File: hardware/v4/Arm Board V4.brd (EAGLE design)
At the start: 114.3 x 50.8 mm, 57 parts, among them IC3 L6206D, U1 SN74LS241DW, U2 XBEE-1B3, U3 LSM9DS0

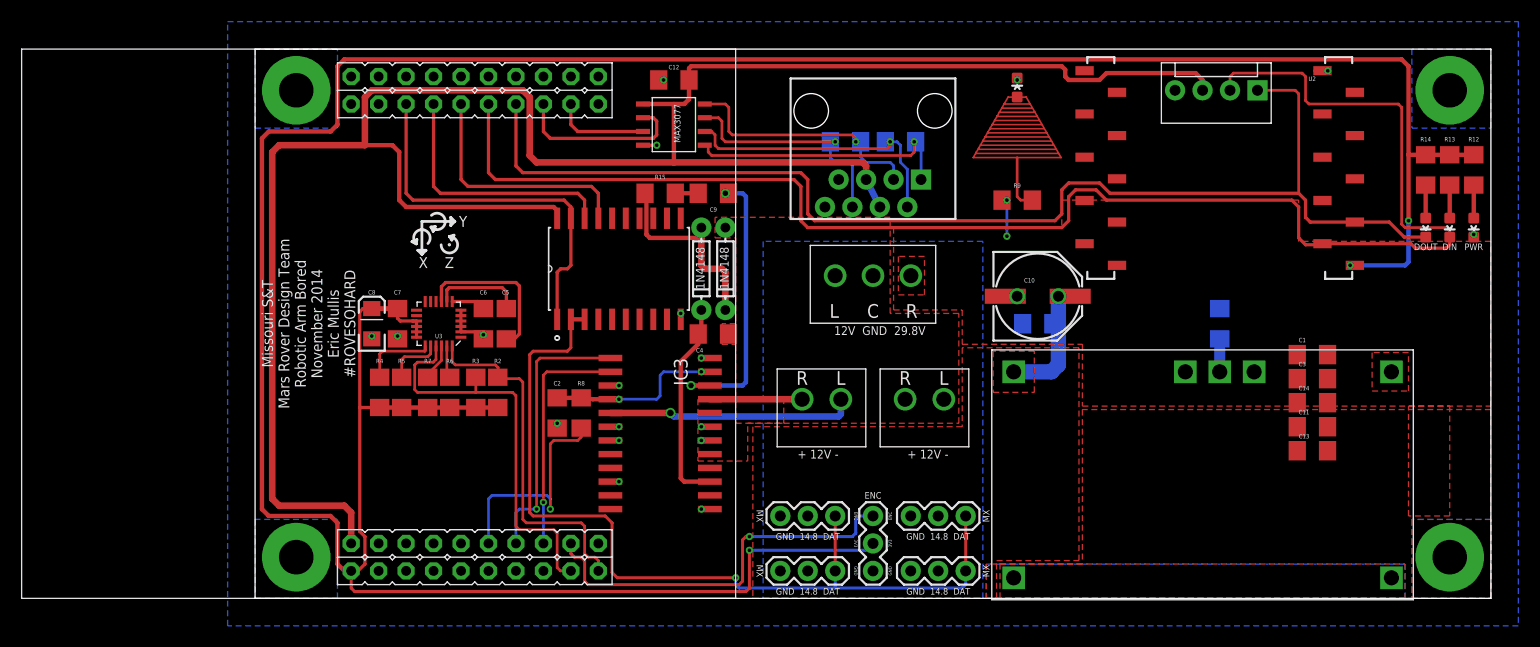
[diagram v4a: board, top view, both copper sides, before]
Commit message: Positioned all the caps correctly
I think the board is finished but may change as I look for parts to make
sure everything is correct
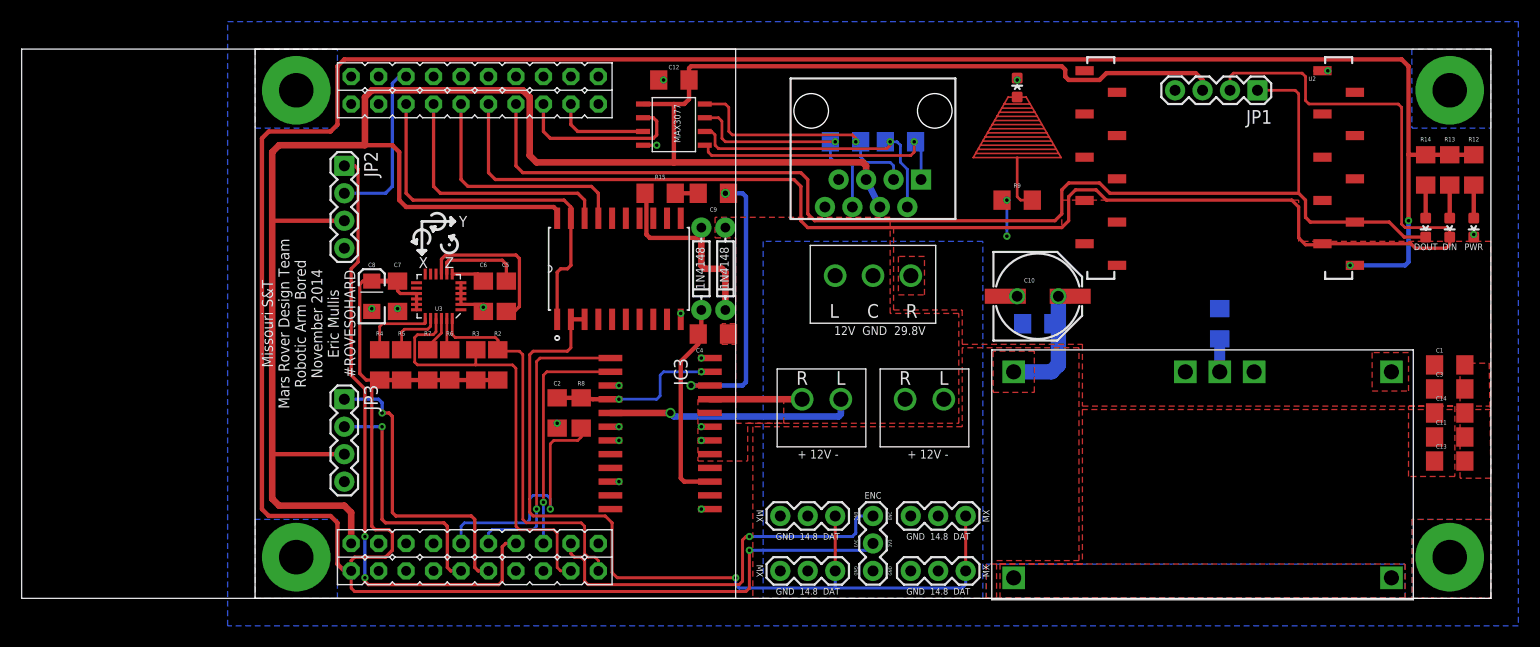
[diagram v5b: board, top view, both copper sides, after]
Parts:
- added JP2, JP3: (no value), SparkFun-Connectors:1X04
- JP1: device SparkFun-Connectors:MOLEX-1X4 -> SparkFun-Connectors:1X04
- moved C1 12.7 mm to (110.5, 21.6)
- moved C11 12.7 mm to (110.5, 14.9)
- moved C13 12.7 mm to (110.5, 12.7)
- moved C14 12.7 mm to (110.5, 17.1)
- moved C3 12.7 mm to (110.5, 19.4)
- moved C5 2.54 mm to (23.2, 27.9)
- moved C6 2.54 mm to (21.1, 27.9)
- moved C7 2.54 mm to (13.2, 27.9)
- moved C8 2.54 mm to (10.8, 27.9)
- moved U3 2.54 mm to (17.0, 27.9)
- moved R2 2.54 mm to (22.4, 21.6)
- moved R3 2.54 mm to (20.4, 21.6)
- moved R4 2.54 mm to (11.5, 21.6)
- moved R5 2.54 mm to (13.6, 21.6)
- moved R6 2.54 mm to (18.0, 21.6)
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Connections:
- new net RX_7: JP2.2, U$1.PE0
- new net TX_7: JP2.1, U$1.PE1
- net +5V: now also JP2.3, JP3.3
- net EN_A: now also U$1.PD2; no longer U$1.PD3
- net GND: now also JP2.4, JP3.4
- net IN1_A: now also U$1.PD3; no longer U$1.PE1
- net RX_5: now also JP3.2
- net TX_5: now also JP3.1
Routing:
- net TX_7: track 0.00 -> 57.8 mm, vias 0 -> 2
- net TX_5: track 0.00 -> 28.3 mm, vias 0 -> 1
- net RX_5: track 0.00 -> 23.6 mm, vias 0 -> 1
- net RX_7: track 0.00 -> 15.8 mm
- net +5V: track 199.1 -> 212.4 mm
- net +3V3: track 293.9 -> 298.6 mm
- net SDA: track 33.4 -> 35.9 mm
- net SCL: track 37.4 -> 40.0 mm
- net IN1_A: track 25.5 -> 27.9 mm
- net EN_A: track 21.0 -> 23.2 mm
- net GND: track 16.9 -> 18.0 mm

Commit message: Cleaned up the part names
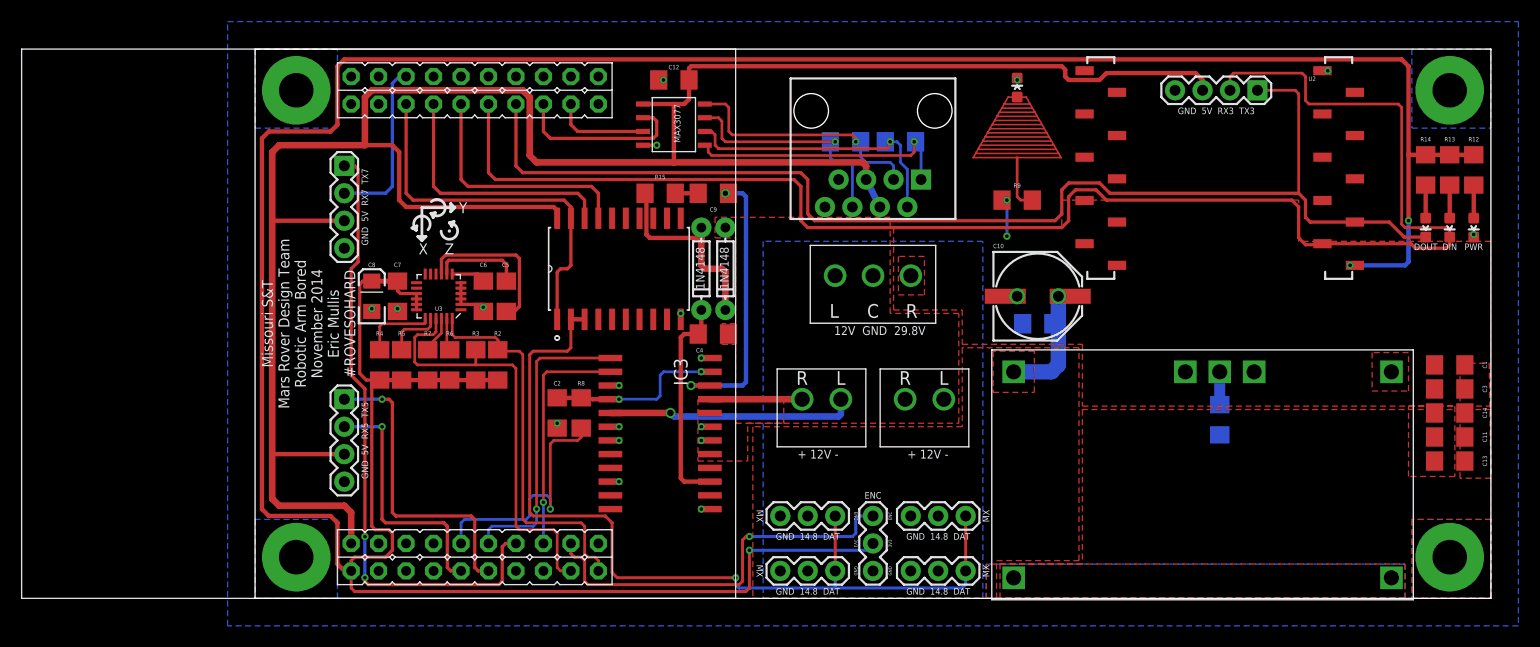
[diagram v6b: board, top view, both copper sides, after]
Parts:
- moved R1 8.89 mm to (89.2, 16.5), turned to 90 degrees
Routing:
- net VBOOT: track 20.1 -> 20.9 mm
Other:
- board text added: "GND 5V RX3 TX3"
- board text added: "GND 5V RX5 TX5"
- board text added: "GND 5V RX7 TX7"

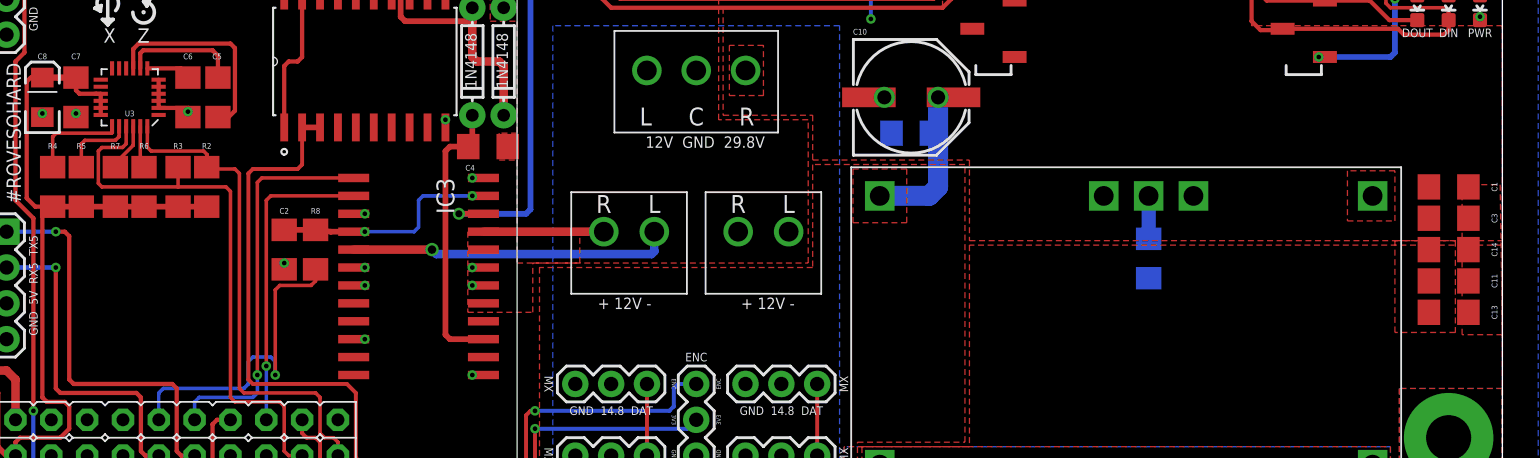
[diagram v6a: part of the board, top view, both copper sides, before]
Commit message: Added Mars Rover Bit Mip
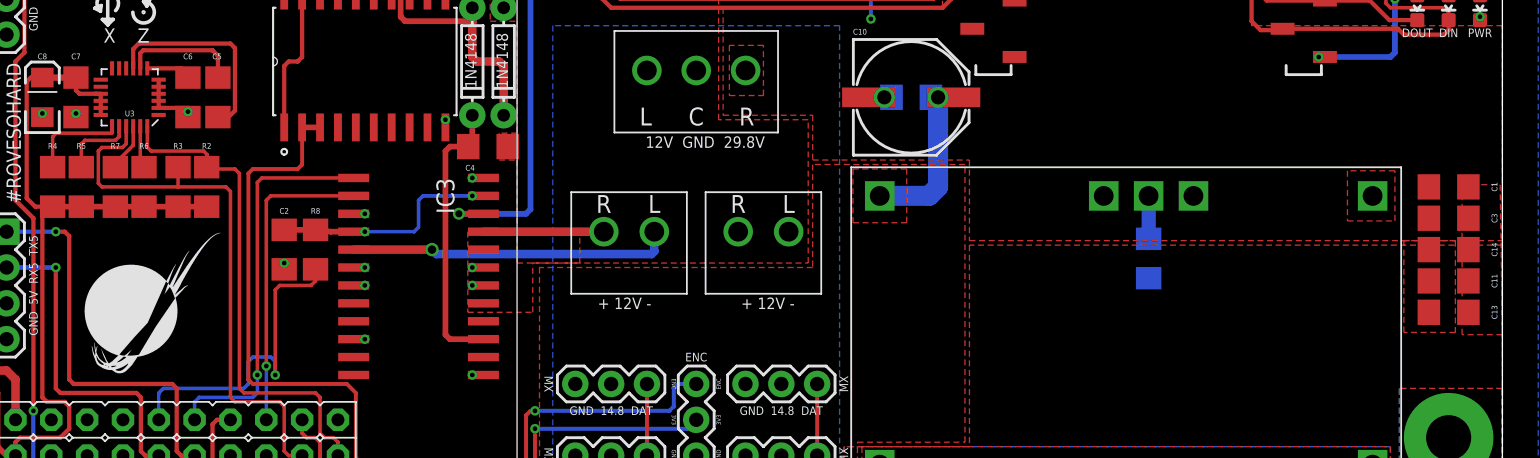
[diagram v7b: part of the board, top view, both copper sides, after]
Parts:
- moved C15 2.54 mm to (72.4, 27.9)

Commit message: 32u4 Xbee Shield
32u4 Xbee Shield
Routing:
- net 14.8V: track 12.4 -> 1.57 mm
- added copper zone on layer 16, net 14.8V
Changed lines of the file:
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@@
 <setting verticaltext="up"/>
 </settings>
-<grid distance="0.05" unitdist="inch" unit="inch" style="lines" multiple="1" display="yes" altdistance="0.0125" altunitdist="inch" altunit="inch"/>
+<grid distance="0.05" unitdist="inch" unit="inch" style="lines" multiple="1" display="yes" altdistance="0.00625" altunitdist="inch" altunit="inch"/>
 <layers>
 <layer number="1" name="Top" color="4" fill="1" visible="yes" active="yes"/>
@@
 <contactref element="JP1" pad="4"/>
 <contactref element="C10" pad="-"/>
-<via x="70.485" y="27.94" extent="1-16" drill="1" shape="square"/>
+<via x="70.64375" y="27.94" extent="1-16" drill="1" shape="square"/>
 <contactref element="C1" pad="2"/>
 <contactref element="C3" pad="2"/>
@@
 <vertex x="114.3" y="11.1125"/>
 </polygon>
-<wire x1="70.485" y1="27.94" x2="69.39" y2="27.94" width="0.254" layer="1"/>
+<wire x1="70.64375" y1="27.94" x2="69.39" y2="27.94" width="0.254" layer="1"/>
 <contactref element="JP3" pad="4"/>
 <contactref element="JP2" pad="4"/>
@@
 <contactref element="JP12" pad="2"/>
 <contactref element="C10" pad="+"/>
-<via x="74.295" y="27.94" extent="1-16" drill="1" shape="square"/>
-<wire x1="74.295" y1="27.94" x2="74.295" y2="21.59" width="1.4224" layer="16"/>
-<wire x1="74.295" y1="21.59" x2="73.66" y2="20.955" width="1.4224" layer="16"/>
-<wire x1="73.66" y1="20.955" x2="70.165" y2="20.955" width="1.4224" layer="16"/>
-<wire x1="70.165" y1="20.955" x2="70.16" y2="20.95" width="1.4224" layer="16"/>
-<wire x1="75.39" y1="27.94" x2="74.295" y2="27.94" width="1.27" layer="1"/>
 <contactref element="C15" pad="1"/>
-<wire x1="73.79" y1="27.94" x2="74.295" y2="27.94" width="0.4064" layer="16"/>
+<polygon width="0.254" layer="16">
+<vertex x="68.58" y="22.86"/>
+<vertex x="68.58" y="19.05"/>
+<vertex x="75.565" y="19.05"/>
+<vertex x="75.565" y="29.5275"/>
+<vertex x="72.0725" y="29.5275"/>
+<vertex x="72.0725" y="22.86"/>
+</polygon>
+<via x="73.81875" y="27.94" extent="1-16" drill="1" shape="square"/>
+<wire x1="73.81875" y1="27.94" x2="75.39" y2="27.94" width="0.254" layer="1"/>
 </signal>
 <signal name="VIN">
